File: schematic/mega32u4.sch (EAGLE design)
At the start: 38 parts, among them Q1 16 MHz, T1 BC847

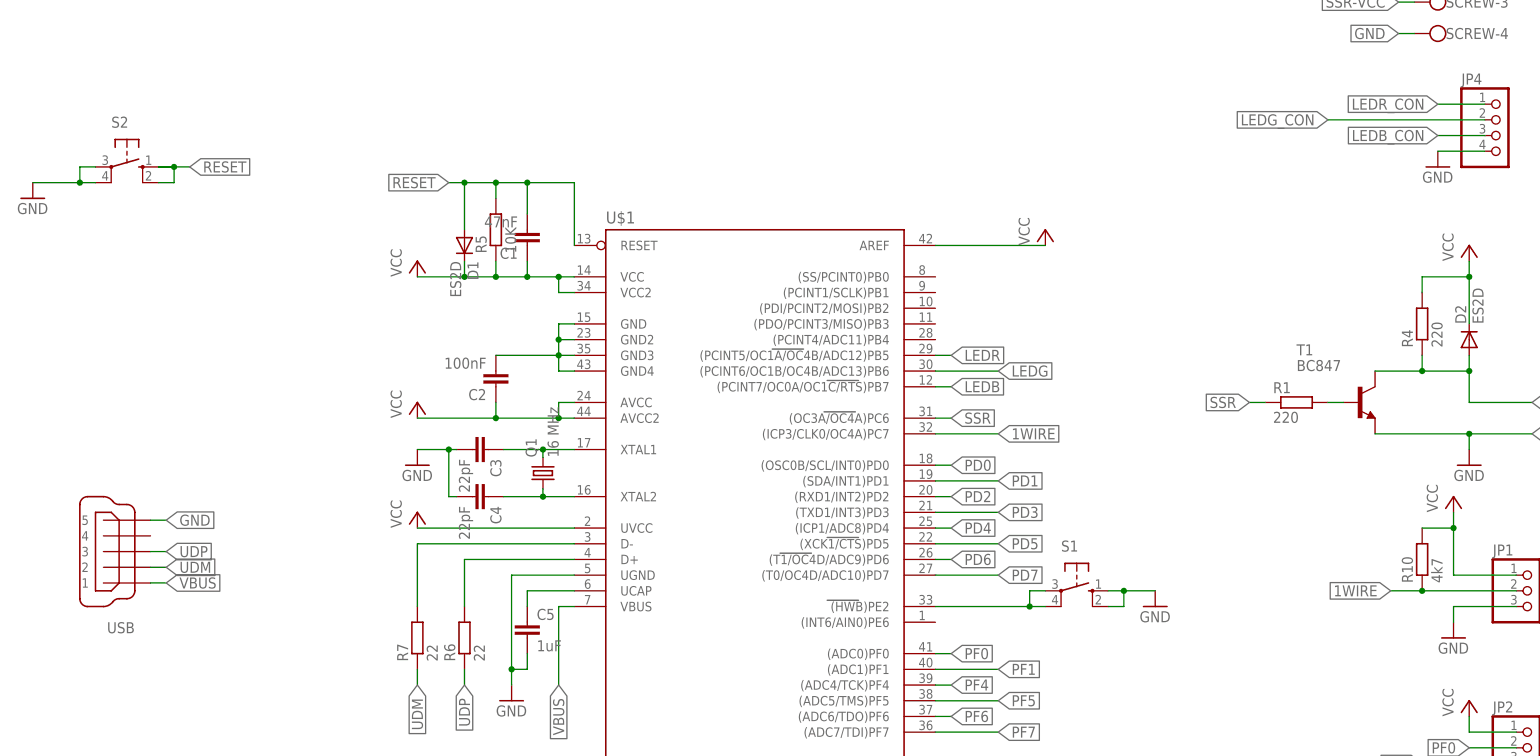
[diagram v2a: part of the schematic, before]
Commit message: Labels modified
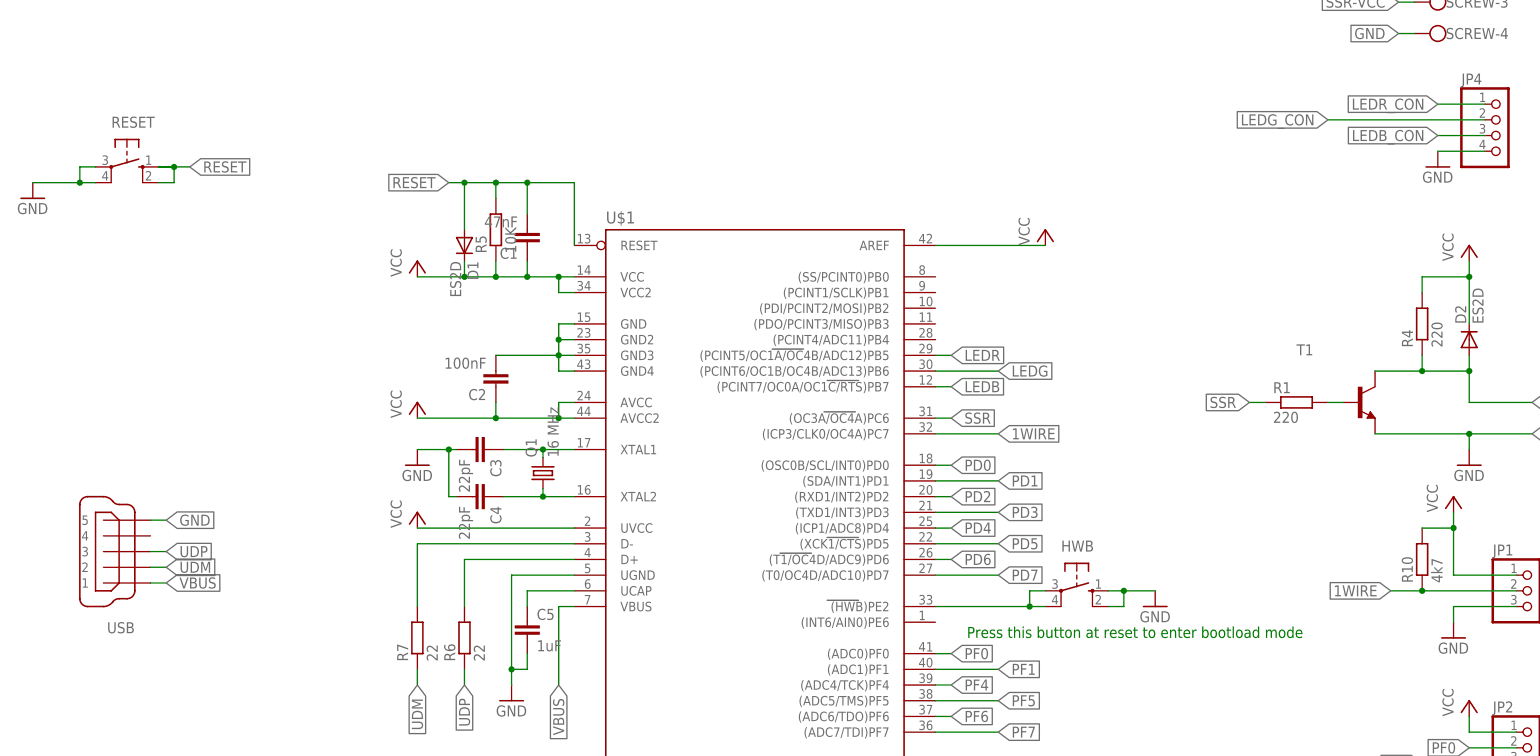
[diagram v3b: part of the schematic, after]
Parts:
- T1: value BC847 -> (none); device transistor:BC847 -> transistor-neu-to92:BC817-25-NPN-SOT23-BEC
- renumbered S1 to HWB, S2 to RESET
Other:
- note added: "Press this button at reset to enter bootload mode"
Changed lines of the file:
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@@
 <part name="C5" library="resistor" deviceset="C-EU" device="C0805K" value="1uF"/>
 <part name="P+4" library="supply1" deviceset="VCC" device=""/>
-<part name="T1" library="transistor" deviceset="BC847" device=""/>
 <part name="R4" library="resistor" deviceset="R-EU_" device="R0805" value="220"/>
 <part name="R5" library="resistor" deviceset="R-EU_" device="R0805" value="10K"/>
@@
 <part name="P+6" library="supply1" deviceset="VCC" device=""/>
 <part name="GND5" library="supply1" deviceset="GND" device=""/>
-<part name="S1" library="switch-omron" deviceset="10-XX" device=""/>
+<part name="HWB" library="switch-omron" deviceset="10-XX" device=""/>
 <part name="GND2" library="supply1" deviceset="GND" device=""/>
 <part name="JP2" library="pinhead" deviceset="PINHD-1X8" device=""/>
@@
 <part name="Q1" library="crystal" deviceset="CRYSTAL" device="CTS406" value="16 MHz"/>
 <part name="USB" library="con-cypressindustries" deviceset="MINI-USB-" device="32005-201" value=""/>
-<part name="S2" library="switch-omron" deviceset="10-XX" device="">
+<part name="RESET" library="switch-omron" deviceset="10-XX" device="">
 <attribute name="MF" value=""/>
 <attribute name="MPN" value="B3F-1000"/>
@@
 <part name="P+10" library="supply1" deviceset="VCC" device=""/>
 <part name="P+11" library="supply1" deviceset="VCC" device=""/>
+<part name="T1" library="transistor-neu-to92" deviceset="*-NPN-" device="SOT23-BEC" technology="BC817-25"/>
 </parts>
 <sheets>
 <sheet>
 <plain>
+<text x="231.14" y="121.92" size="1.778" layer="91">Press this button at reset to enter bootload mode</text>
 </plain>
 <instances>
@@
 <instance part="C5" gate="G$1" x="160.02" y="124.46"/>
 <instance part="P+4" gate="VCC" x="243.84" y="187.96"/>
-<instance part="T1" gate="G$1" x="294.64" y="160.02"/>
 <instance part="R4" gate="G$1" x="304.8" y="172.72" rot="R90"/>
 <instance part="R5" gate="G$1" x="154.94" y="187.96" rot="R90"/>
@@
 <instance part="P+6" gate="VCC" x="309.88" y="144.78"/>
 <instance part="GND5" gate="1" x="309.88" y="121.92"/>
-<instance part="S1" gate="1" x="248.92" y="129.54" rot="R270"/>
+<instance part="HWB" gate="1" x="248.92" y="129.54" rot="R270"/>
 <instance part="GND2" gate="1" x="261.62" y="127"/>
 <instance part="JP2" gate="A" x="322.58" y="96.52"/>
@@
 <instance part="Q1" gate="G$1" x="162.56" y="148.59" rot="R90"/>
 <instance part="USB" gate="G$1" x="93.98" y="135.89" rot="R180"/>
-<instance part="S2" gate="1" x="95.25" y="198.12" rot="R270"/>
+<instance part="RESET" gate="1" x="95.25" y="198.12" rot="R270"/>
 <instance part="GND7" gate="1" x="80.01" y="193.04"/>
 <instance part="JP3" gate="A" x="322.58" y="58.42"/>
@@
 <instance part="P+10" gate="VCC" x="373.38" y="160.02"/>
 <instance part="P+11" gate="VCC" x="353.06" y="256.54"/>
+<instance part="T1" gate="G$1" x="294.64" y="160.02"/>
 </instances>
 <busses>
@@
 </segment>
 <segment>
-<pinref part="S2" gate="1" pin="S1"/>
+<pinref part="RESET" gate="1" pin="S1"/>
 <wire x1="100.33" y1="195.58" x2="102.87" y2="195.58" width="0.1524" layer="91"/>
 <wire x1="102.87" y1="195.58" x2="102.87" y2="198.12" width="0.1524" layer="91"/>
-<pinref part="S2" gate="1" pin="S"/>
+<pinref part="RESET" gate="1" pin="S"/>
 <wire x1="102.87" y1="198.12" x2="100.33" y2="198.12" width="0.1524" layer="91"/>
 <wire x1="100.33" y1="198.12" x2="102.87" y2="198.12" width="0.1524" layer="91"/>
@@
 </segment>
 <segment>
-<pinref part="T1" gate="G$1" pin="E"/>
 <wire x1="297.18" y1="154.94" x2="312.42" y2="154.94" width="0.1524" layer="91"/>
 <wire x1="322.58" y1="154.94" x2="312.42" y2="154.94" width="0.1524" layer="91"/>
@@
 <junction x="312.42" y="154.94"/>
 <label x="322.58" y="154.94" size="1.778" layer="95" xref="yes"/>
+<pinref part="T1" gate="G$1" pin="E"/>
 </segment>
 <segment>
@@
 </segment>
 <segment>
-<pinref part="S1" gate="1" pin="S1"/>
+<pinref part="HWB" gate="1" pin="S1"/>
 <wire x1="254" y1="127" x2="256.54" y2="127" width="0.1524" layer="91"/>
 <wire x1="256.54" y1="127" x2="256.54" y2="129.54" width="0.1524" layer="91"/>
 <pinref part="GND2" gate="1" pin="GND"/>
 <wire x1="256.54" y1="129.54" x2="261.62" y2="129.54" width="0.1524" layer="91"/>
-<pinref part="S1" gate="1" pin="S"/>
+<pinref part="HWB" gate="1" pin="S"/>
 <wire x1="256.54" y1="129.54" x2="254" y2="129.54" width="0.1524" layer="91"/>
 <junction x="256.54" y="129.54"/>
@@
 <segment>
 <pinref part="GND7" gate="1" pin="GND"/>
-<pinref part="S2" gate="1" pin="P1"/>
+<pinref part="RESET" gate="1" pin="P1"/>
 <wire x1="80.01" y1="195.58" x2="87.63" y2="195.58" width="0.1524" layer="91"/>
 <wire x1="90.17" y1="195.58" x2="87.63" y2="195.58" width="0.1524" layer="91"/>
 <wire x1="87.63" y1="195.58" x2="87.63" y2="198.12" width="0.1524" layer="91"/>
-<pinref part="S2" gate="1" pin="P"/>
+<pinref part="RESET" gate="1" pin="P"/>
 <wire x1="87.63" y1="198.12" x2="90.17" y2="198.12" width="0.1524" layer="91"/>
 <junction x="87.63" y="195.58"/>
@@
 <net name="N$5" class="0">
 <segment>
-<pinref part="T1" gate="G$1" pin="B"/>
 <wire x1="289.56" y1="160.02" x2="292.1" y2="160.02" width="0.1524" layer="91"/>
 <pinref part="R1" gate="G$1" pin="2"/>
+<pinref part="T1" gate="G$1" pin="B"/>
 </segment>
 </net>
@@
 <segment>
 <pinref part="U$1" gate="G$1" pin="(HWB)PE2"/>
-<pinref part="S1" gate="1" pin="P1"/>
+<pinref part="HWB" gate="1" pin="P1"/>
 <wire x1="226.06" y1="127" x2="241.3" y2="127" width="0.1524" layer="91"/>
 <wire x1="243.84" y1="127" x2="241.3" y2="127" width="0.1524" layer="91"/>
 <wire x1="241.3" y1="127" x2="241.3" y2="129.54" width="0.1524" layer="91"/>
-<pinref part="S1" gate="1" pin="P"/>
+<pinref part="HWB" gate="1" pin="P"/>
 <wire x1="241.3" y1="129.54" x2="243.84" y2="129.54" width="0.1524" layer="91"/>
 <junction x="241.3" y="127"/>
@@
 </segment>
 <segment>
-<pinref part="T1" gate="G$1" pin="C"/>
 <wire x1="297.18" y1="165.1" x2="304.8" y2="165.1" width="0.1524" layer="91"/>
 <wire x1="304.8" y1="165.1" x2="312.42" y2="165.1" width="0.1524" layer="91"/>
@@
 <junction x="304.8" y="165.1"/>
 <label x="322.58" y="160.02" size="1.778" layer="95" xref="yes"/>
-</segment>
-</net>
+<pinref part="T1" gate="G$1" pin="C"/>
+</segment>
+</net>

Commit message: minor changes
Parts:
- renumbered LED1 to POWER
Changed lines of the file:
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@@
 <part name="R2" library="resistor" deviceset="R-EU_" device="R0805" value="220"/>
 <part name="C6" library="resistor" deviceset="C-EU" device="C0805K" value="47nF"/>
-<part name="LED1" library="led" deviceset="LED" device="SML0805"/>
+<part name="POWER" library="led" deviceset="LED" device="SML0805"/>
 <part name="C8" library="resistor" deviceset="CPOL-EU" device="150CLZ-0810" value="470uF"/>
 <part name="GND8" library="supply1" deviceset="GND" device=""/>
@@
 <instance part="R2" gate="G$1" x="41.91" y="205.74" rot="R90"/>
 <instance part="C6" gate="G$1" x="55.88" y="220.98" rot="R270"/>
-<instance part="LED1" gate="G$1" x="41.91" y="222.25"/>
+<instance part="POWER" gate="G$1" x="41.91" y="222.25"/>
 <instance part="C8" gate="G$1" x="53.34" y="205.74" rot="R90"/>
 <instance part="GND8" gate="1" x="58.42" y="181.61"/>
@@
 </segment>
 <segment>
-<pinref part="LED1" gate="G$1" pin="A"/>
+<pinref part="POWER" gate="G$1" pin="A"/>
 <pinref part="P+8" gate="VCC" pin="VCC"/>
 <wire x1="41.91" y1="224.79" x2="41.91" y2="228.6" width="0.1524" layer="91"/>
@@
 <segment>
 <pinref part="R2" gate="G$1" pin="2"/>
-<pinref part="LED1" gate="G$1" pin="C"/>
+<pinref part="POWER" gate="G$1" pin="C"/>
 <wire x1="41.91" y1="210.82" x2="41.91" y2="217.17" width="0.1524" layer="91"/>
 </segment>

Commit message: bug fixes
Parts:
- added TP1, TP2, TP3, TP4: TPTP10R, testpad:TPTP10R
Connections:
- new net N$12: TP2.TP, U$1.(PDI/PCINT2/MOSI)PB2
- new net N$17: TP3.TP, U$1.(PDO/PCINT3/MISO)PB3
- net GND: now also C2.2, U$1.GND, U$1.GND2, U$1.GND3, U$1.GND4
- net N$1: now also TP1.TP, U$1.(PCINT1/SCLK)PB1; no longer C2.2, U$1.GND, U$1.GND2, U$1.GND3, U$1.GND4
- net RESET: now also TP4.TP
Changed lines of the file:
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@@
 <part name="P+11" library="supply1" deviceset="VCC" device=""/>
 <part name="T1" library="transistor-neu-to92" deviceset="*-NPN-" device="SOT23-BEC" technology="BC817-25"/>
+<part name="GND10" library="supply1" deviceset="GND" device=""/>
+<part name="TP4" library="testpad" deviceset="TP" device="TP10R"/>
+<part name="TP1" library="testpad" deviceset="TP" device="TP10R"/>
+<part name="TP2" library="testpad" deviceset="TP" device="TP10R"/>
+<part name="TP3" library="testpad" deviceset="TP" device="TP10R"/>
 </parts>
 <sheets>
@@
 <instance part="P+11" gate="VCC" x="353.06" y="256.54"/>
 <instance part="T1" gate="G$1" x="294.64" y="160.02"/>
+<instance part="GND10" gate="1" x="160.02" y="162.56"/>
+<instance part="TP4" gate="G$1" x="167.64" y="198.12"/>
+<instance part="TP1" gate="G$1" x="231.14" y="180.34"/>
+<instance part="TP2" gate="G$1" x="233.68" y="177.8"/>
+<instance part="TP3" gate="G$1" x="236.22" y="175.26"/>
 </instances>
 <busses>
@@
 <junction x="149.86" y="195.58"/>
 <pinref part="R5" gate="G$1" pin="2"/>
+<pinref part="TP4" gate="G$1" pin="TP"/>
+<junction x="167.64" y="195.58"/>
 </segment>
 <segment>
@@
 </segment>
 </net>
-<net name="N$1" class="0">
-<segment>
-<pinref part="U$1" gate="G$1" pin="GND"/>
-<wire x1="167.64" y1="172.72" x2="165.1" y2="172.72" width="0.1524" layer="91"/>
-<pinref part="U$1" gate="G$1" pin="GND4"/>
-<wire x1="165.1" y1="172.72" x2="165.1" y2="170.18" width="0.1524" layer="91"/>
-<wire x1="165.1" y1="170.18" x2="165.1" y2="167.64" width="0.1524" layer="91"/>
-<wire x1="165.1" y1="167.64" x2="165.1" y2="165.1" width="0.1524" layer="91"/>
-<wire x1="165.1" y1="165.1" x2="167.64" y2="165.1" width="0.1524" layer="91"/>
-<pinref part="U$1" gate="G$1" pin="GND3"/>
-<wire x1="167.64" y1="167.64" x2="165.1" y2="167.64" width="0.1524" layer="91"/>
-<pinref part="U$1" gate="G$1" pin="GND2"/>
-<wire x1="167.64" y1="170.18" x2="165.1" y2="170.18" width="0.1524" layer="91"/>
-<wire x1="154.94" y1="167.64" x2="165.1" y2="167.64" width="0.1524" layer="91"/>
-<junction x="165.1" y="170.18"/>
-<junction x="165.1" y="167.64"/>
-<pinref part="C2" gate="G$1" pin="2"/>
-</segment>
-</net>
 <net name="N$2" class="0">
 <segment>
@@
 <pinref part="GND9" gate="1" pin="GND"/>
 </segment>
+<segment>
+<pinref part="U$1" gate="G$1" pin="GND4"/>
+<wire x1="160.02" y1="165.1" x2="165.1" y2="165.1" width="0.1524" layer="91"/>
+<pinref part="GND10" gate="1" pin="GND"/>
+<pinref part="U$1" gate="G$1" pin="GND"/>
+<wire x1="165.1" y1="165.1" x2="167.64" y2="165.1" width="0.1524" layer="91"/>
+<wire x1="167.64" y1="172.72" x2="165.1" y2="172.72" width="0.1524" layer="91"/>
+<wire x1="165.1" y1="172.72" x2="165.1" y2="170.18" width="0.1524" layer="91"/>
+<pinref part="U$1" gate="G$1" pin="GND2"/>
+<wire x1="167.64" y1="170.18" x2="165.1" y2="170.18" width="0.1524" layer="91"/>
+<pinref part="U$1" gate="G$1" pin="GND3"/>
+<wire x1="165.1" y1="170.18" x2="165.1" y2="167.64" width="0.1524" layer="91"/>
+<wire x1="167.64" y1="167.64" x2="165.1" y2="167.64" width="0.1524" layer="91"/>
+<wire x1="165.1" y1="167.64" x2="165.1" y2="165.1" width="0.1524" layer="91"/>
+<pinref part="C2" gate="G$1" pin="2"/>
+<wire x1="154.94" y1="167.64" x2="154.94" y2="170.18" width="0.1524" layer="91"/>
+<wire x1="154.94" y1="170.18" x2="165.1" y2="170.18" width="0.1524" layer="91"/>
+<junction x="165.1" y="170.18"/>
+<junction x="165.1" y="167.64"/>
+<junction x="165.1" y="165.1"/>
+</segment>
 </net>
 <net name="N$4" class="0">
@@
 </segment>
 </net>
+<net name="N$1" class="0">
+<segment>
+<pinref part="TP1" gate="G$1" pin="TP"/>
+<pinref part="U$1" gate="G$1" pin="(PCINT1/SCLK)PB1"/>
+<wire x1="231.14" y1="177.8" x2="226.06" y2="177.8" width="0.1524" layer="91"/>
+</segment>
+</net>
+<net name="N$12" class="0">
+<segment>
+<pinref part="TP2" gate="G$1" pin="TP"/>
+<pinref part="U$1" gate="G$1" pin="(PDI/PCINT2/MOSI)PB2"/>
+<wire x1="233.68" y1="175.26" x2="226.06" y2="175.26" width="0.1524" layer="91"/>
+</segment>
+</net>
+<net name="N$17" class="0">
+<segment>
+<pinref part="TP3" gate="G$1" pin="TP"/>
+<pinref part="U$1" gate="G$1" pin="(PDO/PCINT3/MISO)PB3"/>
+<wire x1="236.22" y1="172.72" x2="226.06" y2="172.72" width="0.1524" layer="91"/>
+</segment>
+</net>
